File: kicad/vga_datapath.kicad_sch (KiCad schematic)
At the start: 28 parts, among them Q3 BC547, Q4 BC547, Q5 BC547, U21 74HC377, U23 27C64, U24 74HC166, U27 62256, U30 74HC377, U32 74HC157

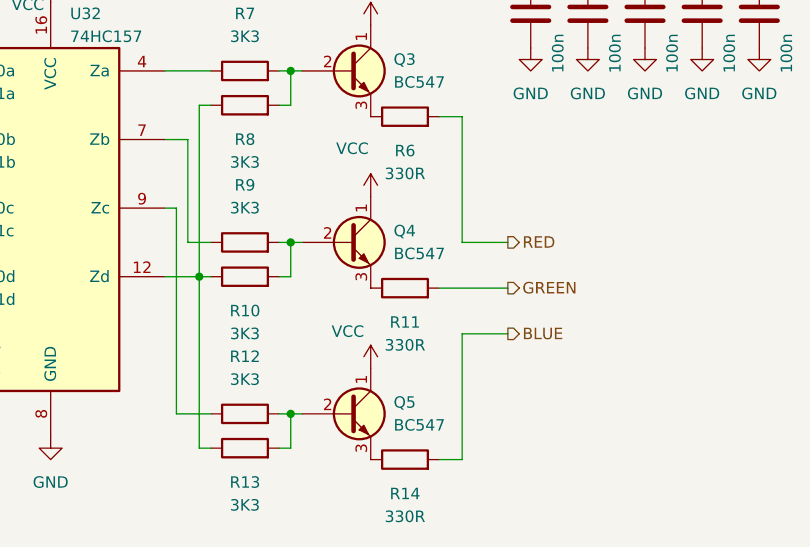
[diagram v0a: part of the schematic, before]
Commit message: Fix wrong D-SUB footprints, rev C
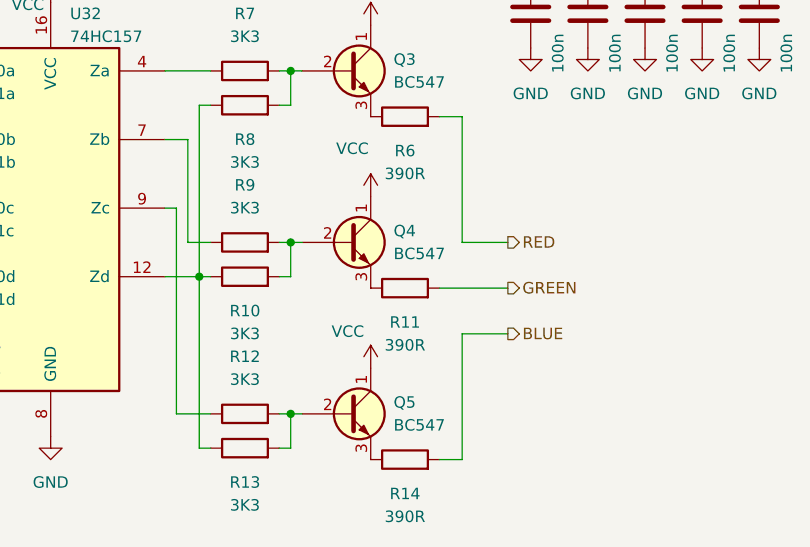
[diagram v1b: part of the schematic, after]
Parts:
- R11, R14, R6: value 330R -> 390R
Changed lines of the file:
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@@
 	(title_block
 		(title "VGA datapath")
-		(date "2025-07-03")
-		(rev "B")
+		(date "2025-07-20")
+		(rev "C")
 		(company "A.K.")
 	)
@@
 			)
 		)
-		(property "Value" "330R"
+		(property "Value" "390R"
 			(at 209.55 115.57 90)
 			(effects
@@
 			)
 		)
-		(property "Value" "330R"
+		(property "Value" "390R"
 			(at 209.55 134.62 90)
 			(effects
@@
 			)
 		)
-		(property "Value" "330R"
+		(property "Value" "390R"
 			(at 209.55 153.67 90)
 			(effects
